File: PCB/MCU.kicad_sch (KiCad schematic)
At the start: 57 parts, among them J4 SWD, J5 SSD1306, Q13 AO3404A, SW1 EC11E15244G1, U12 FT234XD, U2 STM32G474CEUx, Y1 8M

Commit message: Revision 2; gate diodes, 5V into LT, i2c and uart lines fixed
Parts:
- removed D25: LED, LED_SMD:LED_0603_1608Metric, symbol Device:LED
- removed R96: 1k, Resistor_SMD:R_0402_1005Metric, symbol Device:R

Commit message: Changed inductor to much better one
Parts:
- removed D15: APTD1608LQBC/D, Altium_port:kingbright_0603_blue, symbol 0_PD240W:APTD1608LQBC/D
- added D30, D31: LED, LED_SMD:LED_0603_1608Metric, symbol Device:LED
- added R81: 1k, Resistor_SMD:R_0402_1005Metric, symbol Device:R_Small
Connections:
- net +3V3: now also D30.2 (A)
- net GND: now also R81.1
- net at R58.1: now also D30.1 (K)
- net at U2.38 (PA15): now also D31.2 (A)
- new net: D31.1 (K), R81.2

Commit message: Rev2 done, on to ordering
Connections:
- net Reset: now reaches C77.1, R33.2, U2.7 (PG10)
- net Reset: now also J4.3 (Pin_3)
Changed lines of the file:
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@@
 	(wire
 		(pts
+			(xy 323.85 40.64) (xy 328.93 40.64)
+		)
+		(stroke
+			(width 0)
+			(type default)
+		)
+	)
+	(wire
+		(pts
 			(xy 82.55 259.08) (xy 87.63 259.08)
 		)
@@
 		)
 	)
+	(label "Reset"
+		(at 323.85 40.64 180)
+		(effects
+			(font
+				(size 1.27 1.27)
+			)
+			(justify right bottom)
+		)
+	)
 	(label "ENC_B"
 		(at 96.52 259.08 0)
@@
 		(effects
 			(font
+				(size 1.27 1.27)
+			)
+			(justify right bottom)
+		)
+	)
+	(label "Reset"
+		(at 231.14 102.87 180)
+		(effects
+			(font

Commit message: Messed up i2c again, fixed it
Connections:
- net I2C0_SCL: now also R59.1, U2.46 (PB8); no longer U2.16 (PC4)
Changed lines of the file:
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@@
 	)
 	(junction
+		(at 210.82 163.83)
+		(diameter 0)
+		(color 0 0 0 0)
+	)
+	(junction
 		(at 163.83 110.49)
 		(diameter 0)
@@
 	(wire
 		(pts
+			(xy 198.12 163.83) (xy 210.82 163.83)
+		)
+		(stroke
+			(width 0)
+			(type default)
+		)
+	)
+	(wire
+		(pts
 			(xy 44.45 254) (xy 44.45 256.54)
 		)
@@
 	(wire
 		(pts
-			(xy 231.14 123.19) (xy 234.95 123.19)
-		)
-		(stroke
-			(width 0)
-			(type default)
-		)
-	)
-	(wire
-		(pts
 			(xy 161.29 170.18) (xy 157.48 170.18)
 		)
@@
 		)
 	)
+	(label "I2C0_SCL"
+		(at 198.12 163.83 180)
+		(effects
+			(font
+				(size 1.27 1.27)
+			)
+			(justify right bottom)
+		)
+	)
 	(label "I2C0_SDA"
 		(at 167.64 177.8 0)
@@
 		(effects
 			(font
-				(size 1.27 1.27)
-			)
-			(justify right bottom)
-		)
-	)
-	(label "I2C0_SCL"
-		(at 231.14 123.19 180)
-		(effects
-			(font

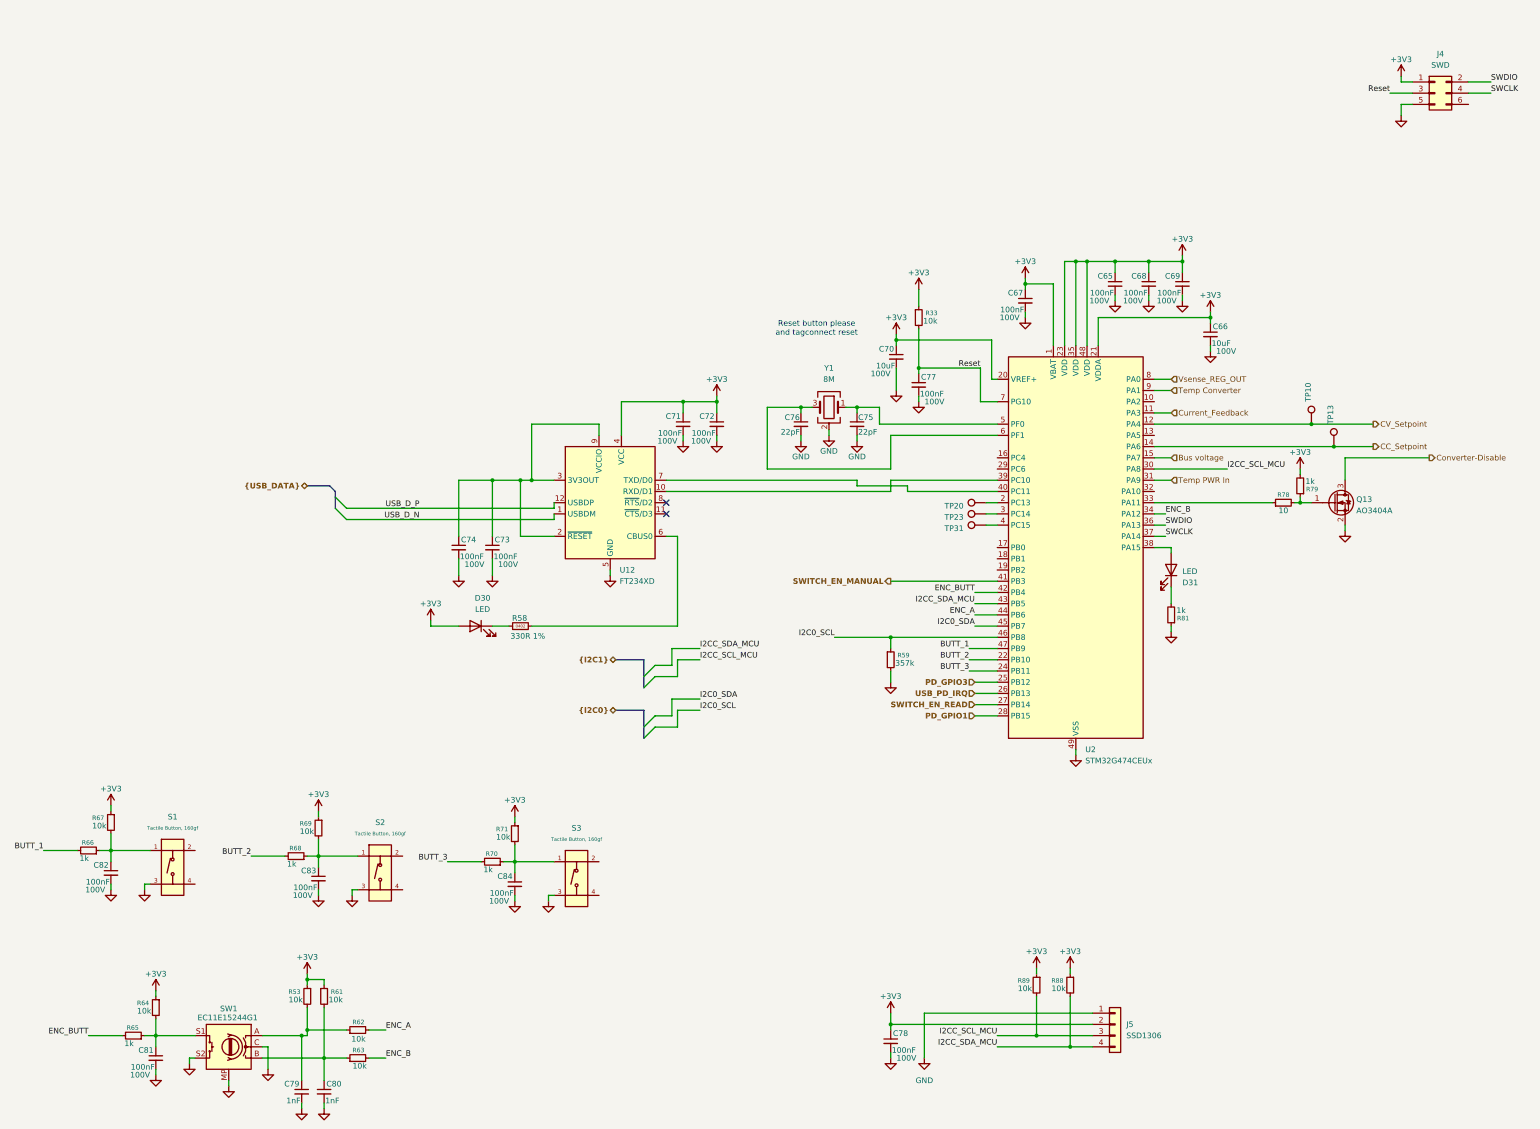
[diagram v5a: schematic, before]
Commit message: Added NMOS output switch (rated for 20A this time)
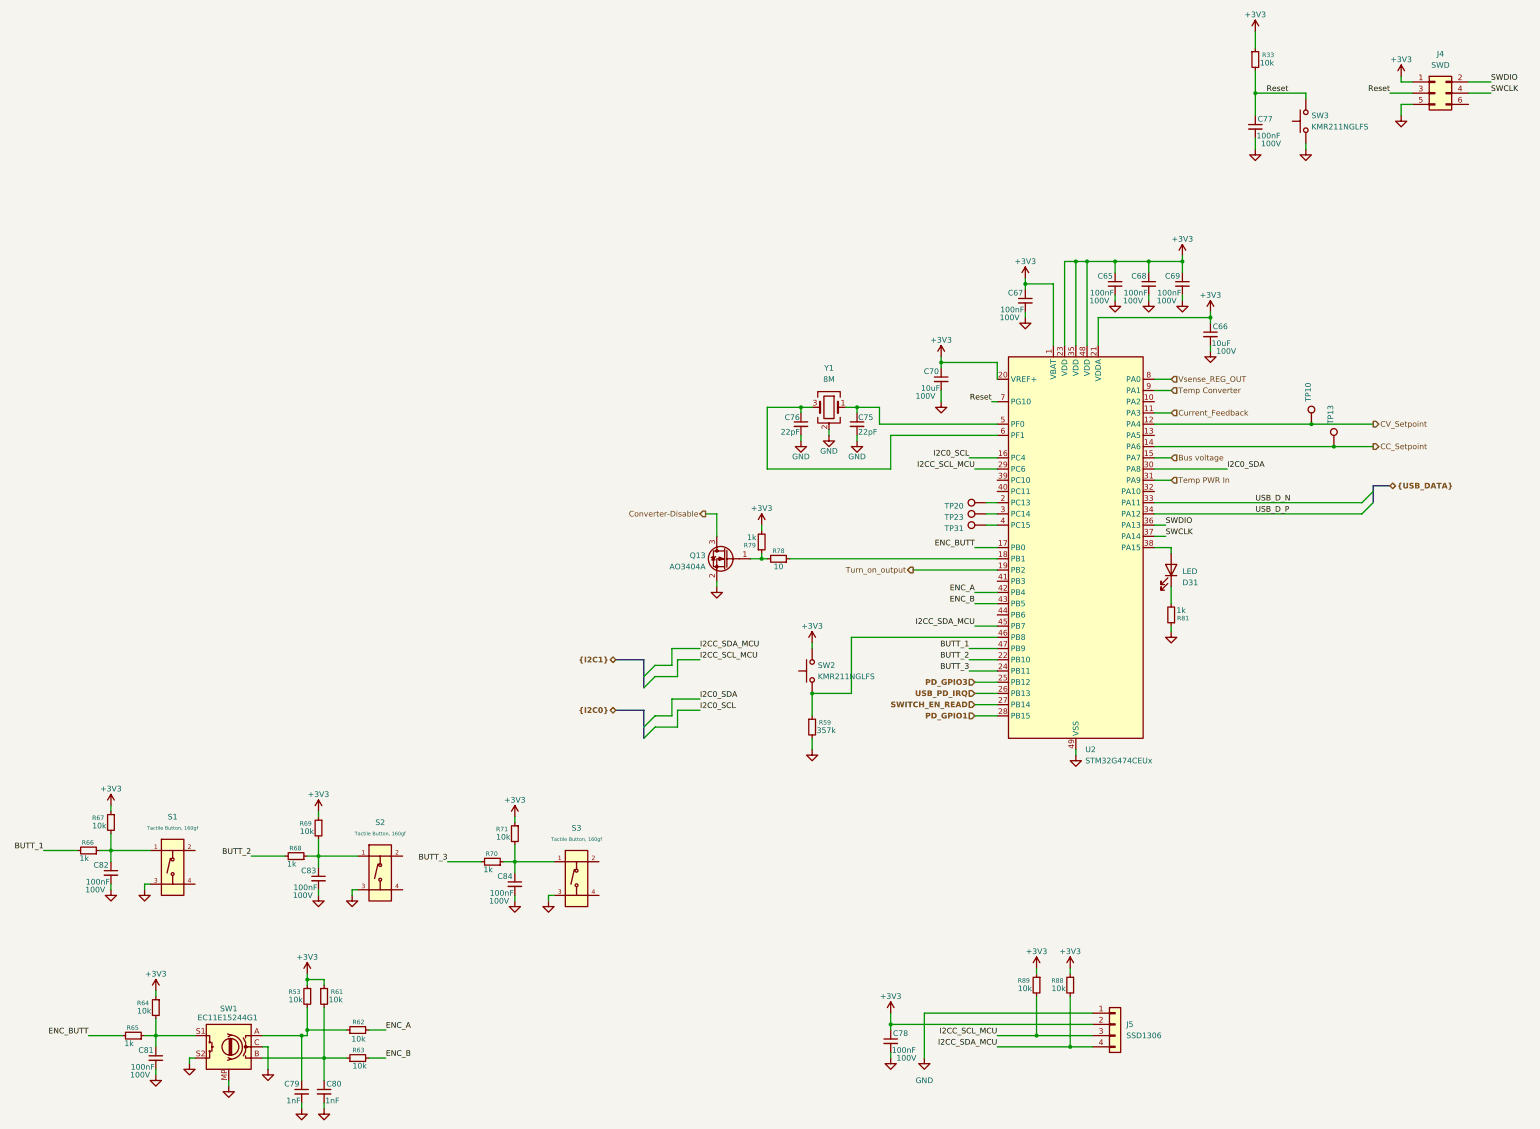
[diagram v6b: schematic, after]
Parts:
- removed C71, C72, C73, C74: 100nF, Capacitor_SMD:C_0402_1005Metric, symbol Device:C_Small
- removed D30: LED, LED_SMD:LED_0603_1608Metric, symbol Device:LED
- removed R58: 330R 1%, Resistor_SMD:R_0402_1005Metric, symbol 0_passives:R_0402
- removed U12: FT234XD, Package_DFN_QFN:WDFN-12-1EP_3x3mm_P0.45mm_EP1.7x2.5mm, symbol Interface_USB:FT234XD
- added SW2, SW3: KMR211NGLFS, Button_Switch_SMD:SW_Push_1P1T_NO_CK_KMR2, symbol Switch:SW_Push
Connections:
- net +3V3: now also SW2.2
- net ENC_A: now also U2.42 (PB4); no longer U2.44 (PB6)
- net ENC_B: now also U2.43 (PB5); no longer U2.34 (PA12)
- net ENC_BUTT: now also U2.17 (PB0); no longer U2.42 (PB4)
- net GND: now also SW3.1
- net I2C0_SCL: now also U2.16 (PC4); no longer R59.1, U2.46 (PB8)
- net I2C0_SDA: now also U2.30 (PA8); no longer U2.45 (PB7)
- net I2CC_SCL_MCU: now also U2.29 (PC6); no longer U2.30 (PA8)
- net I2CC_SDA_MCU: now also U2.45 (PB7); no longer U2.43 (PB5)
- net Reset: now also SW3.2
- net USB_D_N: now also U2.33 (PA11)
- net USB_D_P: now also U2.34 (PA12)
- net at R78.1: now also U2.18 (PB1); no longer U2.33 (PA11)
- net Turn_on_output: now reaches U2.19 (PB2)
- net SWITCH_EN_MANUAL: no longer names the net of U2.41 (PB3)
- new net: R59.1, SW2.1, U2.46 (PB8)
- no-connect marks 2 -> 0
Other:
- note removed: "Reset button please and tagconnect reset"
- moved on the sheet: C70, Q13, R59, R78, R79

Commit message: High current CC calibration
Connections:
- net Converter-on-LOADEN: now reaches U2.41 (PB3)
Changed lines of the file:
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@@
+	(wire
+		(pts
+			(xy 215.9 151.13) (xy 234.95 151.13)
+		)
+		(stroke
+			(width 0)
+			(type default)
+		)
+	)
 	(wire
 		(pts
@@
 		)
 	)
+	(hierarchical_label "Converter-on-LOADEN"
+		(shape output)
+		(at 215.9 151.13 180)
+		(effects
+			(font
+				(size 1.27 1.27)
+			)
+			(justify right)
+		)
+	)

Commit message: Preliminary finish of Rev3
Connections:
- net Sel_high_gain: now reaches U2.44 (PB6)
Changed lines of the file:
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@@
+	(wire
+		(pts
+			(xy 214.63 158.75) (xy 234.95 158.75)
+		)
+		(stroke
+			(width 0)
+			(type default)
+		)
+	)
 	(wire
 		(pts
@@
 		)
 	)
+	(hierarchical_label "Sel_high_gain"
+		(shape output)
+		(at 214.63 158.75 180)
+		(effects
+			(font
+				(size 1.27 1.27)
+			)
+			(justify right)
+		)
+	)
